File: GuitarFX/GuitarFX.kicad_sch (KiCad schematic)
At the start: 0 parts

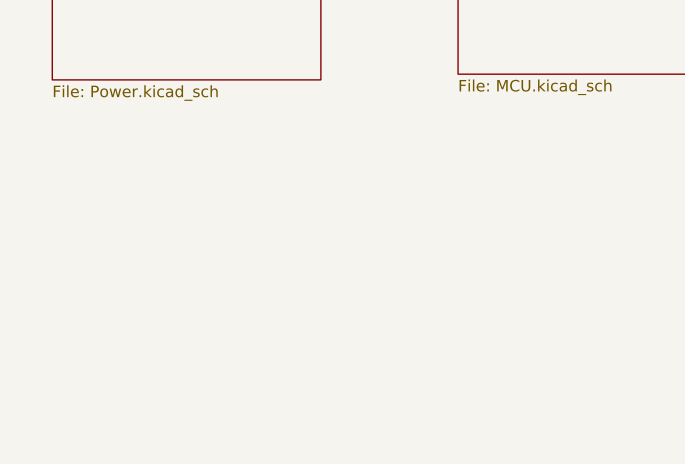
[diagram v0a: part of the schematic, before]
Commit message: Added mounting holes
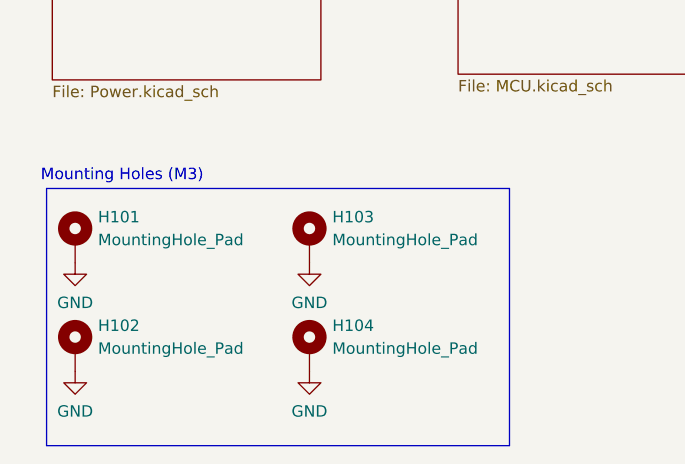
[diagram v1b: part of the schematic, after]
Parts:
- added H101, H102, H103, H104: MountingHole_Pad, MountingHole:MountingHole_3.2mm_M3_Pad, symbol Mechanical:MountingHole_Pad
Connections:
- new net GND: H101.1, H102.1, H103.1, H104.1
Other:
- note added: "Mounting Holes (M3)"
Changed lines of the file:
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@@
     (date "2024-07-23")
+  )
+  (rectangle (start 26.67 96.52) (end 78.105 125.095)
+    (stroke (width 0) (type default))
+    (fill (type none))
   )
   (text "[1] Power" (at 26.035 52.705 0)
@@
     (effects (font (size 4 4) (thickness 2) bold italic) (justify left bottom))
   )
+  (text "Mounting Holes (M3)" (at 26.035 95.885 0)
+    (effects (font (size 1.27 1.27)) (justify left bottom))
+  )
   (text "[3] Codec" (at 115.57 52.07 0)
     (effects (font (size 4 4) (thickness 2) bold italic) (justify left bottom))
   )
+  (symbol (lib_id "power:GND") (at 29.845 104.775 0) (unit 1)
+    (in_bom yes) (on_board yes) (dnp no) (fields_autoplaced)
+    (property "Reference" "#PWR0101" (at 29.845 111.125 0)
+      (effects (font (size 1.27 1.27)) hide)
+    )
+    (property "Value" "GND" (at 29.845 109.22 0)
+      (effects (font (size 1.27 1.27)))
+    )
+    (property "Footprint" "" (at 29.845 104.775 0)
+      (effects (font (size 1.27 1.27)) hide)
+    )
+    (property "Datasheet" "" (at 29.845 104.775 0)
+      (effects (font (size 1.27 1.27)) hide)
+    )
+    (pin "1")
+    (instances
+      (project "GuitarFX"
+        (path "/4ab4bfc6-98ca-4cb1-8273-436b96035b51"
+          (reference "#PWR0101") (unit 1)
+        )
+      )
+    )
+  )
+  (symbol (lib_id "Mechanical:MountingHole_Pad") (at 29.845 114.3 0) (unit 1)
+    (in_bom yes) (on_board yes) (dnp no) (fields_autoplaced)
+    (property "Reference" "H102" (at 32.385 111.76 0)
+      (effects (font (size 1.27 1.27)) (justify left))
+    )
+    (property "Value" "MountingHole_Pad" (at 32.385 114.3 0)
+      (effects (font (size 1.27 1.27)) (justify left))
+    )
+    (property "Footprint" "MountingHole:MountingHole_3.2mm_M3_Pad" (at 29.845 114.3 0)
+      (effects (font (size 1.27 1.27)) hide)
+    )
+    (property "Datasheet" "~" (at 29.845 114.3 0)
+      (effects (font (size 1.27 1.27)) hide)
+    )
+    (pin "1")
+    (instances
+      (project "GuitarFX"
+        (path "/4ab4bfc6-98ca-4cb1-8273-436b96035b51"
+          (reference "H102") (unit 1)
+        )
+      )
+    )
+  )
+  (symbol (lib_id "Mechanical:MountingHole_Pad") (at 55.88 102.235 0) (unit 1)
+    (in_bom yes) (on_board yes) (dnp no) (fields_autoplaced)
+    (property "Reference" "H103" (at 58.42 99.695 0)
+      (effects (font (size 1.27 1.27)) (justify left))
+    )
+    (property "Value" "MountingHole_Pad" (at 58.42 102.235 0)
+      (effects (font (size 1.27 1.27)) (justify left))
+    )
+    (property "Footprint" "MountingHole:MountingHole_3.2mm_M3_Pad" (at 55.88 102.235 0)
+      (effects (font (size 1.27 1.27)) hide)
+    )
+    (property "Datasheet" "~" (at 55.88 102.235 0)
+      (effects (font (size 1.27 1.27)) hide)
+    )
+    (pin "1")
+    (instances
+      (project "GuitarFX"
+        (path "/4ab4bfc6-98ca-4cb1-8273-436b96035b51"
+          (reference "H103") (unit 1)
+        )
+      )
+    )
+  )
+  (symbol (lib_id "power:GND") (at 55.88 104.775 0) (unit 1)
+    (in_bom yes) (on_board yes) (dnp no) (fields_autoplaced)
+    (property "Reference" "#PWR0103" (at 55.88 111.125 0)
+      (effects (font (size 1.27 1.27)) hide)
+    )
+    (property "Value" "GND" (at 55.88 109.22 0)
+      (effects (font (size 1.27 1.27)))
+    )
+    (property "Footprint" "" (at 55.88 104.775 0)
+      (effects (font (size 1.27 1.27)) hide)
+    )
+    (property "Datasheet" "" (at 55.88 104.775 0)
+      (effects (font (size 1.27 1.27)) hide)
+    )
+    (pin "1")
+    (instances
+      (project "GuitarFX"
+        (path "/4ab4bfc6-98ca-4cb1-8273-436b96035b51"
+          (reference "#PWR0103") (unit 1)
+        )
+      )
+    )
+  )
+  (symbol (lib_id "power:GND") (at 55.88 116.84 0) (unit 1)
+    (in_bom yes) (on_board yes) (dnp no) (fields_autoplaced)
+    (property "Reference" "#PWR0104" (at 55.88 123.19 0)
+      (effects (font (size 1.27 1.27)) hide)
+    )
+    (property "Value" "GND" (at 55.88 121.285 0)
+      (effects (font (size 1.27 1.27)))
+    )
+    (property "Footprint" "" (at 55.88 116.84 0)
+      (effects (font (size 1.27 1.27)) hide)
+    )
+    (property "Datasheet" "" (at 55.88 116.84 0)
+      (effects (font (size 1.27 1.27)) hide)
+    )
+    (pin "1")
+    (instances
+      (project "GuitarFX"
+        (path "/4ab4bfc6-98ca-4cb1-8273-436b96035b51"
+          (reference "#PWR0104") (unit 1)
+        )
+      )
+    )
+  )
+  (symbol (lib_id "power:GND") (at 29.845 116.84 0) (unit 1)
+    (in_bom yes) (on_board yes) (dnp no) (fields_autoplaced)
+    (property "Reference" "#PWR0102" (at 29.845 123.19 0)
+      (effects (font (size 1.27 1.27)) hide)
+    )
+    (property "Value" "GND" (at 29.845 121.285 0)
+      (effects (font (size 1.27 1.27)))
+    )
+    (property "Footprint" "" (at 29.845 116.84 0)
+      (effects (font (size 1.27 1.27)) hide)
+    )
+    (property "Datasheet" "" (at 29.845 116.84 0)
+      (effects (font (size 1.27 1.27)) hide)
+    )
+    (pin "1")
+    (instances
+      (project "GuitarFX"
+        (path "/4ab4bfc6-98ca-4cb1-8273-436b96035b51"
+          (reference "#PWR0102") (unit 1)
+        )
+      )
+    )
+  )
+  (symbol (lib_id "Mechanical:MountingHole_Pad") (at 29.845 102.235 0) (unit 1)
+    (in_bom yes) (on_board yes) (dnp no) (fields_autoplaced)
+    (property "Reference" "H101" (at 32.385 99.695 0)
+      (effects (font (size 1.27 1.27)) (justify left))
+    )
+    (property "Value" "MountingHole_Pad" (at 32.385 102.235 0)
+      (effects (font (size 1.27 1.27)) (justify left))
+    )
+    (property "Footprint" "MountingHole:MountingHole_3.2mm_M3_Pad" (at 29.845 102.235 0)
+      (effects (font (size 1.27 1.27)) hide)
+    )
+    (property "Datasheet" "~" (at 29.845 102.235 0)
+      (effects (font (size 1.27 1.27)) hide)
+    )
+    (pin "1")
+    (instances
+      (project "GuitarFX"
+        (path "/4ab4bfc6-98ca-4cb1-8273-436b96035b51"
+          (reference "H101") (unit 1)
+        )
+      )
+    )
+  )
+  (symbol (lib_id "Mechanical:MountingHole_Pad") (at 55.88 114.3 0) (unit 1)
+    (in_bom yes) (on_board yes) (dnp no) (fields_autoplaced)
+    (property "Reference" "H104" (at 58.42 111.76 0)
+      (effects (font (size 1.27 1.27)) (justify left))
+    )
+    (property "Value" "MountingHole_Pad" (at 58.42 114.3 0)
+      (effects (font (size 1.27 1.27)) (justify left))
+    )
+    (property "Footprint" "MountingHole:MountingHole_3.2mm_M3_Pad" (at 55.88 114.3 0)
+      (effects (font (size 1.27 1.27)) hide)
+    )
+    (property "Datasheet" "~" (at 55.88 114.3 0)
+      (effects (font (size 1.27 1.27)) hide)
+    )
+    (pin "1")
+    (instances
+      (project "GuitarFX"
+        (path "/4ab4bfc6-98ca-4cb1-8273-436b96035b51"
+          (reference "H104") (unit 1)
+        )
+      )
+    )
+  )
   (sheet (at 27.305 56.515) (size 29.845 27.94) (fields_autoplaced)

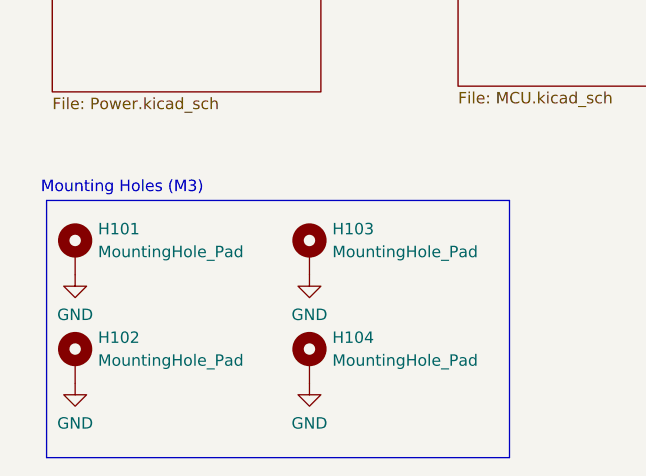
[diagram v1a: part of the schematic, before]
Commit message: Finished 3V power routing
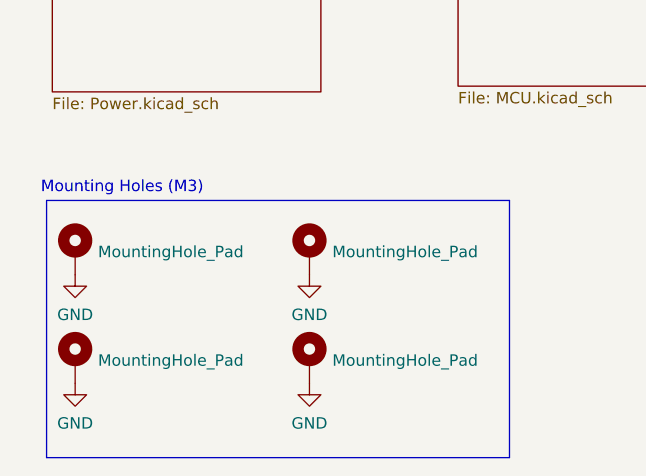
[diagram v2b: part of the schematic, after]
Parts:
- H101, H102, H103, H104: footprint MountingHole:MountingHole_3.2mm_M3_Pad -> MountingHole:MountingHole_3.2mm_M3_Pad_Via; now left out of the parts list
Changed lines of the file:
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@@
   )
   (symbol (lib_id "Mechanical:MountingHole_Pad") (at 29.845 114.3 0) (unit 1)
-    (in_bom yes) (on_board yes) (dnp no) (fields_autoplaced)
+    (in_bom no) (on_board yes) (dnp no) (fields_autoplaced)
     (property "Reference" "H102" (at 32.385 111.76 0)
-      (effects (font (size 1.27 1.27)) (justify left))
+      (effects (font (size 1.27 1.27)) (justify left) hide)
     )
     (property "Value" "MountingHole_Pad" (at 32.385 114.3 0)
       (effects (font (size 1.27 1.27)) (justify left))
     )
-    (property "Footprint" "MountingHole:MountingHole_3.2mm_M3_Pad" (at 29.845 114.3 0)
+    (property "Footprint" "MountingHole:MountingHole_3.2mm_M3_Pad_Via" (at 29.845 114.3 0)
       (effects (font (size 1.27 1.27)) hide)
     )
@@
   )
   (symbol (lib_id "Mechanical:MountingHole_Pad") (at 55.88 102.235 0) (unit 1)
-    (in_bom yes) (on_board yes) (dnp no) (fields_autoplaced)
+    (in_bom no) (on_board yes) (dnp no) (fields_autoplaced)
     (property "Reference" "H103" (at 58.42 99.695 0)
-      (effects (font (size 1.27 1.27)) (justify left))
+      (effects (font (size 1.27 1.27)) (justify left) hide)
     )
     (property "Value" "MountingHole_Pad" (at 58.42 102.235 0)
       (effects (font (size 1.27 1.27)) (justify left))
     )
-    (property "Footprint" "MountingHole:MountingHole_3.2mm_M3_Pad" (at 55.88 102.235 0)
+    (property "Footprint" "MountingHole:MountingHole_3.2mm_M3_Pad_Via" (at 55.88 102.235 0)
       (effects (font (size 1.27 1.27)) hide)
     )
@@
   )
   (symbol (lib_id "Mechanical:MountingHole_Pad") (at 29.845 102.235 0) (unit 1)
-    (in_bom yes) (on_board yes) (dnp no) (fields_autoplaced)
+    (in_bom no) (on_board yes) (dnp no) (fields_autoplaced)
     (property "Reference" "H101" (at 32.385 99.695 0)
-      (effects (font (size 1.27 1.27)) (justify left))
+      (effects (font (size 1.27 1.27)) (justify left) hide)
     )
     (property "Value" "MountingHole_Pad" (at 32.385 102.235 0)
       (effects (font (size 1.27 1.27)) (justify left))
     )
-    (property "Footprint" "MountingHole:MountingHole_3.2mm_M3_Pad" (at 29.845 102.235 0)
+    (property "Footprint" "MountingHole:MountingHole_3.2mm_M3_Pad_Via" (at 29.845 102.235 0)
       (effects (font (size 1.27 1.27)) hide)
     )
@@
   )
   (symbol (lib_id "Mechanical:MountingHole_Pad") (at 55.88 114.3 0) (unit 1)
-    (in_bom yes) (on_board yes) (dnp no) (fields_autoplaced)
+    (in_bom no) (on_board yes) (dnp no) (fields_autoplaced)
     (property "Reference" "H104" (at 58.42 111.76 0)
-      (effects (font (size 1.27 1.27)) (justify left))
+      (effects (font (size 1.27 1.27)) (justify left) hide)
     )
     (property "Value" "MountingHole_Pad" (at 58.42 114.3 0)
       (effects (font (size 1.27 1.27)) (justify left))
     )
-    (property "Footprint" "MountingHole:MountingHole_3.2mm_M3_Pad" (at 55.88 114.3 0)
+    (property "Footprint" "MountingHole:MountingHole_3.2mm_M3_Pad_Via" (at 55.88 114.3 0)
       (effects (font (size 1.27 1.27)) hide)
     )
